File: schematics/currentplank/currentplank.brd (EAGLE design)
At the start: 80 x 49 mm, 24 parts, among them IC1 74AHC1G86DBV, IC2 STCS2A, IC3 STCS2A

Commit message: Work on constant current plank.
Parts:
- removed SJ2, SJ3: (no value), jumper:SJ
- added IC4: OPAMP-DUALU, SparkFun-AnalogIC:SO08
- added R6, R7: 1k, nickparts:TRIMPOT-3MM-2
- R1, R3: value .1 ohm -> 0.05
- R2, R4: value .1 ohm -> 32k; device SparkFun-Passives:1206 -> SparkFun-Passives:0805
- U$1: value LOKI_PLANKLONG -> LOKI_PLANKSHORT; device loki:PLANK_LONG -> loki:PLANK_SHORT
- moved X1 111.7 mm to (42.5, 24.1), turned to 90 degrees
- moved X2 107.5 mm to (7.30, 32.4), turned to 270 degrees
- moved SJ4 105.9 mm to (13.3, 4.45)
- moved R5 102.2 mm to (3.81, 24.4)
- moved R2 98.9 mm to (31.8, 30.5), turned to 90 degrees
- moved X3 98.0 mm to (7.30, 15.9), turned to 270 degrees
- moved R4 92.6 mm to (33.7, 14.9), turned to 270 degrees
- moved R1 92.1 mm to (27.9, 28.6)
- moved R3 84.1 mm to (27.9, 12.1)
- moved C4 81.1 mm to (12.7, 37.1)
- moved D1 80.2 mm to (19.7, 22.9), turned to 180 degrees
- moved C3 78.9 mm to (27.6, 32.4)
- moved C6 75.5 mm to (28.6, 16.5)
- moved C1 59.0 mm to (11.4, 25.7), turned to 90 degrees
- moved C5 57.5 mm to (11.4, 8.89)
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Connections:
- new net DISC2: IC3.10, U$1.I1.2
- new net N$43: R2.1, R6.3
- new net N$44: IC4.5, R7.2
- new net N$45: R4.1, R7.3
- new net N$46: C2.1, C4.1, IC2.1, IC2.3, IC3.1, IC3.3, R5.1
- new net PWM2: IC3.2, U$1.I1.1
- net +3V3: now also IC4.8, R2.2, R4.2
- net DISC1: now also U$1.I2.2; no longer U$1.I1.2
- net GND: now also IC4.4, R6.1, R7.1; no longer R2.2, R4.2
- net N$29: now also IC4.2; no longer IC2.7, SJ2.1
- net N$30: now also IC2.7, IC4.1; no longer R2.1, SJ2.2
- net N$33: now also D1.C, R5.2, SJ4.1; no longer D1.A, X1.1
- net N$35: now also D1.A, X1.1, X2.1, X3.1; no longer D1.C, R5.1, SJ4.1
- net N$36: now also IC4.3, R6.2; no longer C2.1, C4.1, IC2.1, IC2.3, IC3.1, IC3.3, R5.2, X2.2, X3.2
- net N$37: now also X2.2; no longer X2.1
- net N$38: now also X3.2; no longer X3.1
- net N$41: now also IC3.6, IC4.6; no longer IC3.7, SJ3.1
- net N$42: now also IC3.7, IC4.7; no longer R4.1, SJ3.2
- net PWM1: now also U$1.I2.1; no longer U$1.I1.1
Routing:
- net PWM2: track 0.00 -> 91.6 mm, vias 0 -> 1
- net GND: track 36.9 -> 117.6 mm, vias 1 -> 4
- net DISC2: track 0.00 -> 45.8 mm, vias 0 -> 1
- net +3V3: track 40.2 -> 83.4 mm, vias 1 -> 4
- net N$35: track 0.00 -> 40.4 mm
- net N$33: track 0.00 -> 39.8 mm
- net PWM1: track 0.00 -> 24.8 mm, vias 0 -> 1
- net N$41: track 0.00 -> 14.3 mm
- net N$46: track 0.00 -> 13.6 mm
- net N$42: track 0.00 -> 10.9 mm
- net N$44: track 0.00 -> 10.6 mm
- net N$36: track 0.00 -> 9.55 mm
- net N$30: track 0.00 -> 7.85 mm
- net N$38: track 0.00 -> 7.74 mm
- net DISC1: track 0.00 -> 7.65 mm, vias 0 -> 1
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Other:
- board size 80 x 49 mm -> 50 x 49 mm

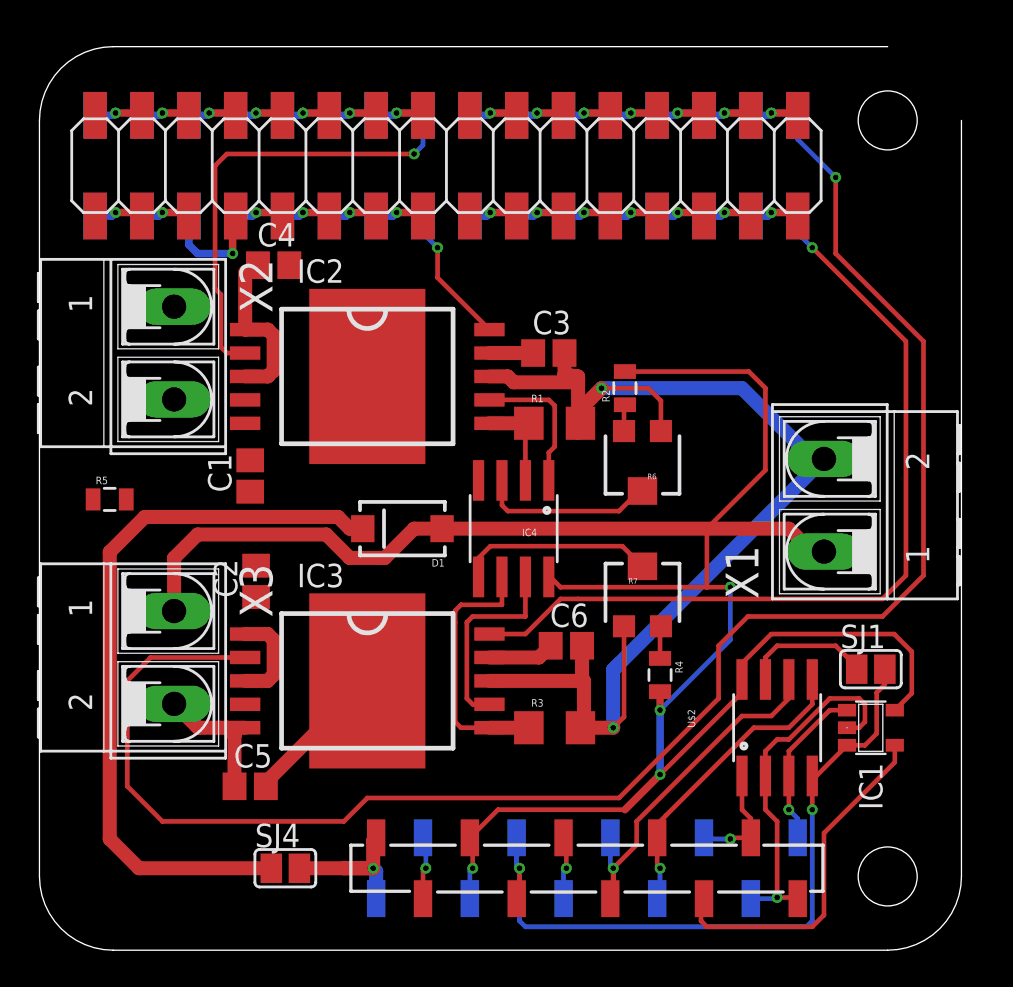
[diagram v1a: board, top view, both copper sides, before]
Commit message: Rework of current plank, now using opamp and trimpot to set current limit.
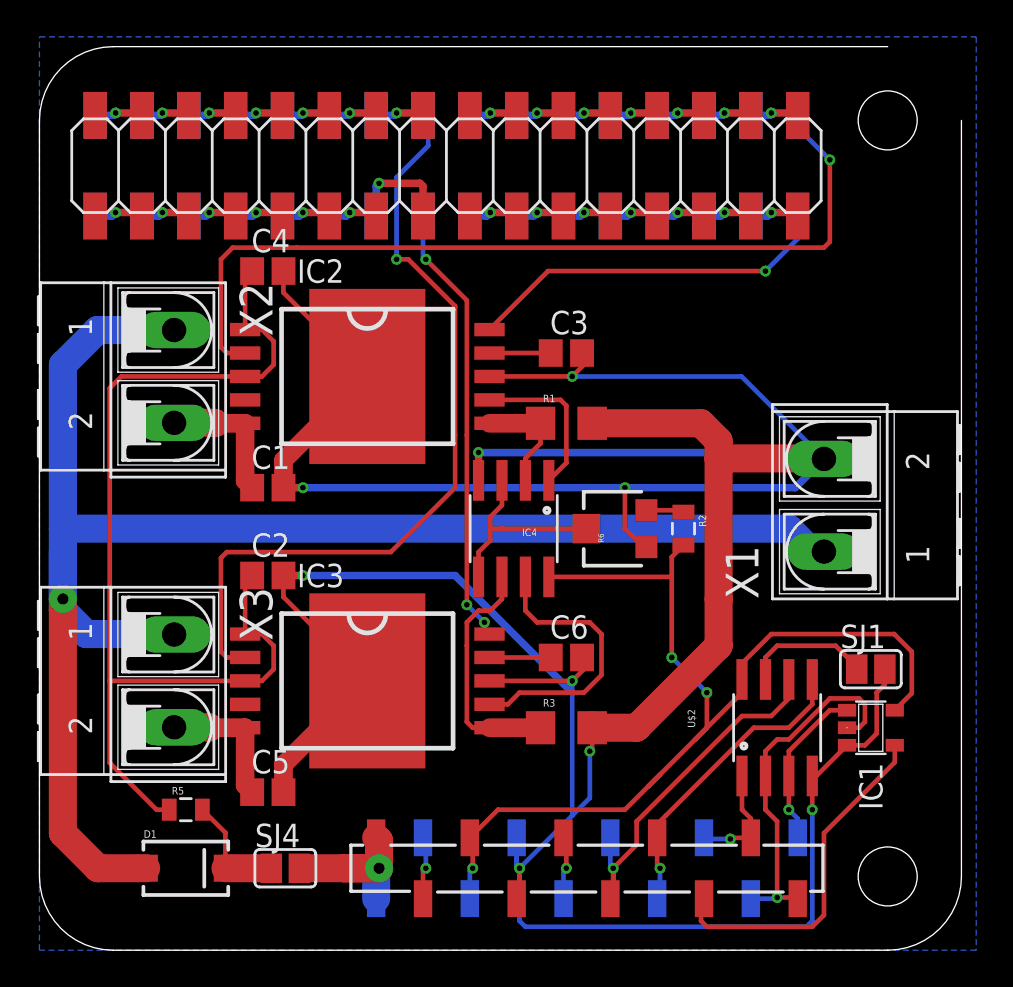
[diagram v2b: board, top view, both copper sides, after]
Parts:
- removed R4: 32k, SparkFun-Passives:0805
- removed R7: 1k, nickparts:TRIMPOT-3MM-2
- moved D1 21.8 mm to (7.94, 4.45), turned to 0 degrees
- moved R5 17.3 mm to (7.94, 7.62)
- moved R2 8.26 mm to (34.9, 22.9), turned to 270 degrees
- moved R6 3.84 mm to (31.1, 22.9), turned to 90 degrees
- moved X2 1.27 mm to (7.30, 31.1)
- moved X3 1.27 mm to (7.30, 14.6)
- moved C1 1.14 mm to (12.4, 25.1), turned to 0 degrees
- moved C5 1.00 mm to (12.4, 8.57)
- moved C3 0.95 mm to (28.6, 32.4)
- moved C2 0.71 mm to (12.4, 20.3), turned to 0 degrees
- moved C6 0.64 mm to (28.6, 15.9)
- moved R1 0.63 mm to (28.6, 28.6)
- moved R3 0.63 mm to (28.6, 12.1)
- moved C4 0.45 mm to (12.4, 36.8)
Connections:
- removed net N$36: IC4.3, R6.2
- removed net N$44: IC4.5, R7.2
- removed net N$45: R4.1, R7.3
- new net CURRENTADJ: IC4.3, IC4.5, R6.2
- net +3V3: no longer R4.2
- net DISC1: now also U$1.I1.2; no longer U$1.I2.2
- net DISC2: now also U$1.I2.2; no longer U$1.I1.2
- net GND: no longer R7.1
- net PWM1: now also U$1.I1.1; no longer U$1.I2.1
- net PWM2: now also U$1.I2.1; no longer U$1.I1.1
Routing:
- net GND: track 117.6 -> 221.5 mm, vias 4 -> 9
- net N$35: track 40.4 -> 89.1 mm, vias 0 -> 1
- net PWM2: track 91.6 -> 43.7 mm
- net N$46: track 13.6 -> 56.3 mm
- net N$33: track 39.8 -> 6.18 mm
- net +3V3: track 83.4 -> 56.3 mm, vias 4 -> 3
- net PWM1: track 24.8 -> 47.2 mm
- net DISC2: track 45.8 -> 24.2 mm, vias 1 -> 3
- net DISC1: track 7.65 -> 20.0 mm
- net CURRENTADJ: track 0.00 -> 11.0 mm
- net N$44: track 10.6 -> 0.00 mm
- net N$36: track 9.55 -> 0.00 mm
- net N$37: track 0.00 -> 7.51 mm
- net N$42: track 10.9 -> 15.4 mm
- net N$19: track 6.23 -> 2.70 mm
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- added copper zone on layer 16, net GND

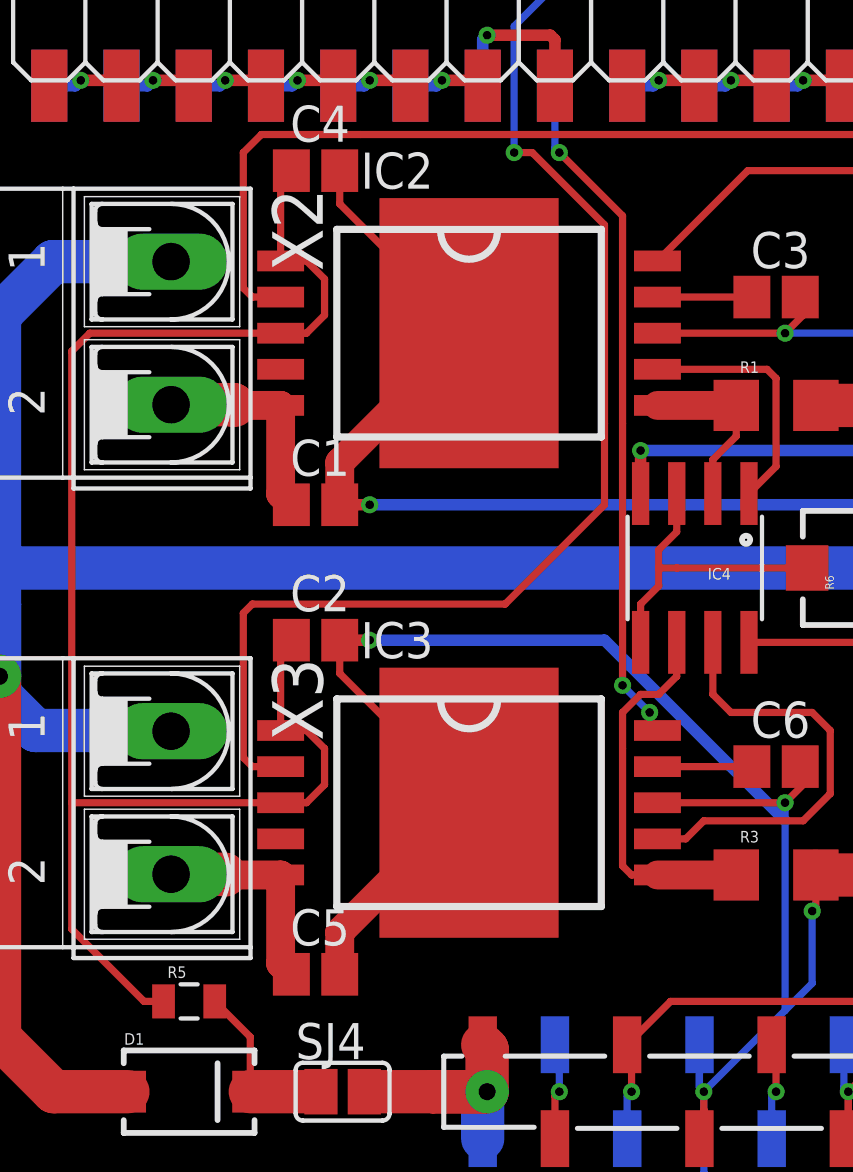
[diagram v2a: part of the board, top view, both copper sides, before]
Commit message: Thermal vias etc for current plank.
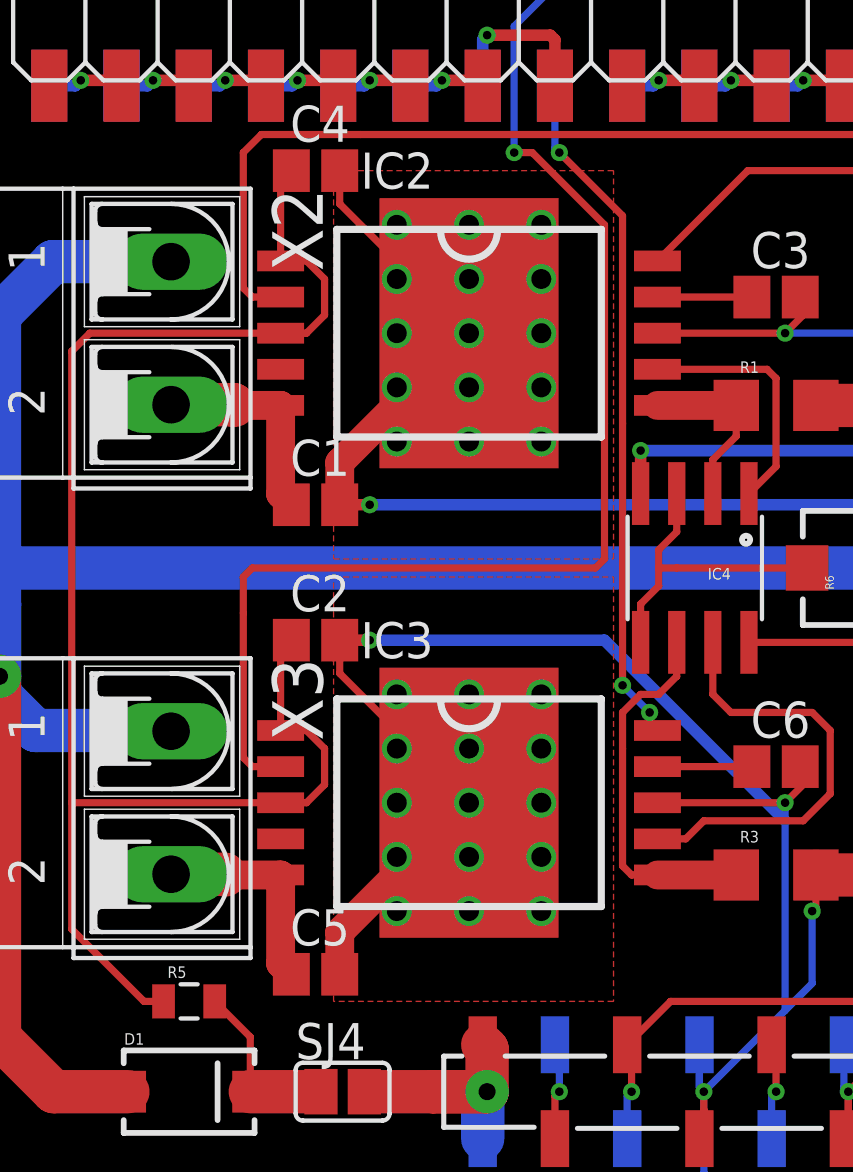
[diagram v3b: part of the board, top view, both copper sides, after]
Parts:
- IC2, IC3: device stcs2a:POWER-SO10 -> currentplank:STCS2A_POWER-SO10
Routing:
- net PWM2: track 43.7 -> 45.5 mm
- net GND: vias 9 -> 39
- added copper zone on layer 1, net GND
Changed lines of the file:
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@@
 </element>
 <element name="SJ1" library="jumper" package="SJ" value="" x="45.085" y="15.24"/>
-<element name="IC2" library="stcs2a" package="POWER-SO10" value="STCS2A" x="17.78" y="31.115"/>
-<element name="IC3" library="stcs2a" package="POWER-SO10" value="STCS2A" x="17.78" y="14.605"/>
+<element name="IC2" library="currentplank" package="STCS2A_POWER-SO10" value="STCS2A" x="17.78" y="31.115"/>
+<element name="IC3" library="currentplank" package="STCS2A_POWER-SO10" value="STCS2A" x="17.78" y="14.605"/>
 <element name="C1" library="resistor" package="C0805" value="1uf 50v" x="12.3825" y="25.0825"/>
 <element name="C2" library="resistor" package="C0805" value=".1uf 50v" x="12.3825" y="20.32"/>
@@
 <wire x1="31.75" y1="22.86" x2="31.75" y2="25.0825" width="0.254" layer="1"/>
 <via x="31.75" y="25.0825" extent="1-16" drill="0.3"/>
+<via x="15.24" y="34.925" extent="1-16" drill="0.7"/>
+<via x="17.78" y="34.925" extent="1-16" drill="0.7"/>
+<via x="20.32" y="34.925" extent="1-16" drill="0.7"/>
+<via x="20.32" y="33.02" extent="1-16" drill="0.7"/>
+<via x="17.78" y="33.02" extent="1-16" drill="0.7"/>
+<via x="15.24" y="33.02" extent="1-16" drill="0.7"/>
+<via x="15.24" y="29.21" extent="1-16" drill="0.7"/>
+<via x="17.78" y="29.21" extent="1-16" drill="0.7"/>
+<via x="20.32" y="29.21" extent="1-16" drill="0.7"/>
+<via x="20.32" y="27.305" extent="1-16" drill="0.7"/>
+<via x="17.78" y="27.305" extent="1-16" drill="0.7"/>
+<via x="15.24" y="27.305" extent="1-16" drill="0.7"/>
+<via x="17.78" y="31.115" extent="1-16" drill="0.7"/>
+<via x="17.78" y="14.605" extent="1-16" drill="0.7"/>
+<via x="15.24" y="31.115" extent="1-16" drill="0.7"/>
+<via x="20.32" y="31.115" extent="1-16" drill="0.7"/>
+<via x="15.24" y="18.415" extent="1-16" drill="0.7"/>
+<via x="17.78" y="18.415" extent="1-16" drill="0.7"/>
+<via x="20.32" y="18.415" extent="1-16" drill="0.7"/>
+<via x="20.32" y="16.51" extent="1-16" drill="0.7"/>
+<via x="17.78" y="16.51" extent="1-16" drill="0.7"/>
+<via x="15.24" y="16.51" extent="1-16" drill="0.7"/>
+<via x="15.24" y="14.605" extent="1-16" drill="0.7"/>
+<via x="20.32" y="14.605" extent="1-16" drill="0.7"/>
+<via x="20.32" y="12.7" extent="1-16" drill="0.7"/>
+<via x="17.78" y="12.7" extent="1-16" drill="0.7"/>
+<via x="15.24" y="12.7" extent="1-16" drill="0.7"/>
+<via x="15.24" y="10.795" extent="1-16" drill="0.7"/>
+<via x="17.78" y="10.795" extent="1-16" drill="0.7"/>
+<via x="20.32" y="10.795" extent="1-16" drill="0.7"/>
+<polygon width="0.254" layer="1">
+<vertex x="22.86" y="7.62"/>
+<vertex x="13.0175" y="7.62"/>
+<vertex x="13.0175" y="22.5425"/>
+<vertex x="22.86" y="22.5425"/>
+</polygon>
+<polygon width="0.254" layer="1">
+<vertex x="13.0175" y="23.1775"/>
+<vertex x="22.86" y="23.1775"/>
+<vertex x="22.86" y="36.83"/>
+<vertex x="13.0175" y="36.83"/>
+</polygon>
 </signal>
 <signal name="A0">
@@
 <wire x1="22.5425" y1="34.925" x2="22.5425" y2="27.94" width="0.254" layer="1"/>
 <wire x1="22.5425" y1="27.94" x2="22.5425" y2="25.0825" width="0.254" layer="1"/>
-<wire x1="22.5425" y1="25.0825" x2="19.05" y2="21.59" width="0.254" layer="1"/>
-<wire x1="19.05" y1="21.59" x2="10.16" y2="21.59" width="0.254" layer="1"/>
-<wire x1="10.16" y1="21.59" x2="9.8425" y2="21.2725" width="0.254" layer="1"/>
 <wire x1="9.8425" y1="21.2725" x2="9.8425" y2="16.1925" width="0.254" layer="1"/>
 <wire x1="9.8425" y1="16.1925" x2="10.16" y2="15.875" width="0.254" layer="1"/>
 <wire x1="10.16" y1="15.875" x2="11.155" y2="15.875" width="0.254" layer="1"/>
+<wire x1="22.5425" y1="25.0825" x2="22.5425" y2="23.1775" width="0.254" layer="1"/>
+<wire x1="22.5425" y1="23.1775" x2="22.225" y2="22.86" width="0.254" layer="1"/>
+<wire x1="22.225" y1="22.86" x2="10.16" y2="22.86" width="0.254" layer="1"/>
+<wire x1="10.16" y1="22.86" x2="9.8425" y2="22.5425" width="0.254" layer="1"/>
+<wire x1="9.8425" y1="22.5425" x2="9.8425" y2="21.2725" width="0.254" layer="1"/>
 </signal>
 <signal name="DISC2">
@@
 </signal>
 </signals>
+<errors>
+</errors>
 </board>
 </drawing>

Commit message: Moar symmetry!
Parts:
- moved X1 1.27 mm to (42.5, 22.9)
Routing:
- net N$35: track 89.1 -> 89.9 mm
- net GND: track 221.5 -> 222.0 mm
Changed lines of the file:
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@@
 <element name="R3" library="SparkFun-Passives" package="1206" value="0.05" x="28.575" y="12.065"/>
 <element name="R5" library="SparkFun-Passives" package="0805" value="100 ohm" x="7.9375" y="7.62"/>
-<element name="X1" library="con-ptr500" package="AK500/2-H" value="" x="42.545" y="24.13" rot="R90">
-<attribute name="OC_NEWARK" value="unknown" x="42.545" y="24.13" size="1.778" layer="27" rot="R90" display="off"/>
-<attribute name="MPN" value="" x="42.545" y="24.13" size="1.778" layer="27" rot="R90" display="off"/>
-<attribute name="MF" value="" x="42.545" y="24.13" size="1.778" layer="27" rot="R90" display="off"/>
-<attribute name="OC_FARNELL" value="unknown" x="42.545" y="24.13" size="1.778" layer="27" rot="R90" display="off"/>
+<element name="X1" library="con-ptr500" package="AK500/2-H" value="" x="42.545" y="22.86" rot="R90">
+<attribute name="OC_NEWARK" value="unknown" x="42.545" y="22.86" size="1.778" layer="27" rot="R90" display="off"/>
+<attribute name="MPN" value="" x="42.545" y="22.86" size="1.778" layer="27" rot="R90" display="off"/>
+<attribute name="MF" value="" x="42.545" y="22.86" size="1.778" layer="27" rot="R90" display="off"/>
+<attribute name="OC_FARNELL" value="unknown" x="42.545" y="22.86" size="1.778" layer="27" rot="R90" display="off"/>
 </element>
 <element name="X2" library="con-ptr500" package="AK500/2-H" value="" x="7.3025" y="31.115" rot="R270">
@@
 <wire x1="13.2325" y1="26.5675" x2="17.78" y2="31.115" width="1.016" layer="1"/>
 <wire x1="29.975" y1="12.065" x2="29.975" y2="12.195" width="1.524" layer="1"/>
-<wire x1="36.83" y1="19.05" x2="36.83" y2="26.67" width="1.524" layer="1"/>
-<wire x1="36.83" y1="26.67" x2="42.5196" y2="26.67" width="1.524" layer="1"/>
-<wire x1="42.5196" y1="26.67" x2="42.545" y2="26.6446" width="1.524" layer="1"/>
+<wire x1="36.83" y1="19.05" x2="36.83" y2="25.4" width="1.524" layer="1"/>
+<wire x1="36.83" y1="25.4" x2="36.83" y2="26.67" width="1.524" layer="1"/>
 <wire x1="36.83" y1="26.67" x2="36.83" y2="27.6225" width="1.524" layer="1"/>
 <wire x1="36.83" y1="27.6225" x2="35.8775" y2="28.575" width="1.524" layer="1"/>
@@
 <via x="28.8925" y="31.115" extent="1-16" drill="0.3"/>
 <wire x1="28.8925" y1="13.97" x2="28.8925" y2="7.3025" width="0.254" layer="16"/>
-<wire x1="28.8925" y1="31.115" x2="38.0746" y2="31.115" width="0.254" layer="16"/>
-<wire x1="38.0746" y1="31.115" x2="42.545" y2="26.6446" width="0.254" layer="16"/>
 <wire x1="23.8125" y1="25.4762" x2="23.8125" y2="26.9875" width="0.4064" layer="1"/>
 <via x="23.8125" y="26.9875" extent="1-16" drill="0.3"/>
-<wire x1="23.8125" y1="26.9875" x2="41.5925" y2="26.9875" width="0.4064" layer="16"/>
-<wire x1="41.5925" y1="26.9875" x2="41.91" y2="26.67" width="0.4064" layer="16"/>
-<wire x1="41.91" y1="26.67" x2="42.5196" y2="26.67" width="0.4064" layer="16"/>
-<wire x1="42.5196" y1="26.67" x2="42.545" y2="26.6446" width="0.4064" layer="16"/>
 <wire x1="13.2325" y1="20.32" x2="14.2875" y2="20.32" width="0.4064" layer="1"/>
 <via x="14.2875" y="20.32" extent="1-16" drill="0.3"/>
@@
 <wire x1="14.2875" y1="25.0825" x2="31.75" y2="25.0825" width="0.4064" layer="16"/>
 <wire x1="31.75" y1="25.0825" x2="40.9829" y2="25.0825" width="0.4064" layer="16"/>
-<wire x1="40.9829" y1="25.0825" x2="42.545" y2="26.6446" width="0.4064" layer="16"/>
 <polygon width="0.4064" layer="16">
 <vertex x="0" y="0"/>
@@
 <vertex x="13.0175" y="36.83"/>
 </polygon>
+<wire x1="42.545" y1="25.3746" x2="36.8554" y2="25.3746" width="1.524" layer="1"/>
+<wire x1="36.8554" y1="25.3746" x2="36.83" y2="25.4" width="1.524" layer="1"/>
+<wire x1="40.9829" y1="25.0825" x2="42.2529" y2="25.0825" width="0.254" layer="16"/>
+<wire x1="42.2529" y1="25.0825" x2="42.545" y2="25.3746" width="0.254" layer="16"/>
+<wire x1="28.8925" y1="31.115" x2="36.8046" y2="31.115" width="0.254" layer="16"/>
+<wire x1="36.8046" y1="31.115" x2="42.545" y2="25.3746" width="0.254" layer="16"/>
+<wire x1="23.8125" y1="26.9875" x2="40.9321" y2="26.9875" width="0.254" layer="16"/>
+<wire x1="40.9321" y1="26.9875" x2="42.545" y2="25.3746" width="0.254" layer="16"/>
 </signal>
 <signal name="A0">
@@
 <contactref element="X1" pad="1"/>
 <contactref element="X2" pad="1"/>
-<wire x1="42.545" y1="21.6154" x2="41.8846" y2="21.6154" width="1.524" layer="16"/>
-<wire x1="41.8846" y1="21.6154" x2="40.64" y2="22.86" width="1.524" layer="16"/>
 <wire x1="40.64" y1="22.86" x2="1.27" y2="22.86" width="1.524" layer="16"/>
 <wire x1="1.27" y1="22.86" x2="1.27" y2="21.59" width="1.524" layer="16"/>
@@
 <via x="1.27" y="19.05" extent="1-16" drill="0.6" diameter="1.524"/>
 <wire x1="1.27" y1="19.05" x2="1.27" y2="21.59" width="1.524" layer="16"/>
+<wire x1="42.545" y1="20.3454" x2="42.545" y2="20.955" width="1.524" layer="16"/>
+<wire x1="42.545" y1="20.955" x2="40.64" y2="22.86" width="1.524" layer="16"/>
 </signal>
 </signals>
